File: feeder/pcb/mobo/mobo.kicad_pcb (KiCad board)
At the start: 2 copper layers, 149.5 x 70 mm, 26 parts, among them J1 SERIAL_BRIDGE, J2 Spring_Finger_Interface, J3 AVR-ISP-6, M1 Motor_DC, SW1 SW_Push, SW2 SW_Push, SW3 SW_Push, SW4 SW_SPDT, U1 ATmega328-AU, U2 VCNT2020, U3 DRV8838, Y1 Resonator_Small

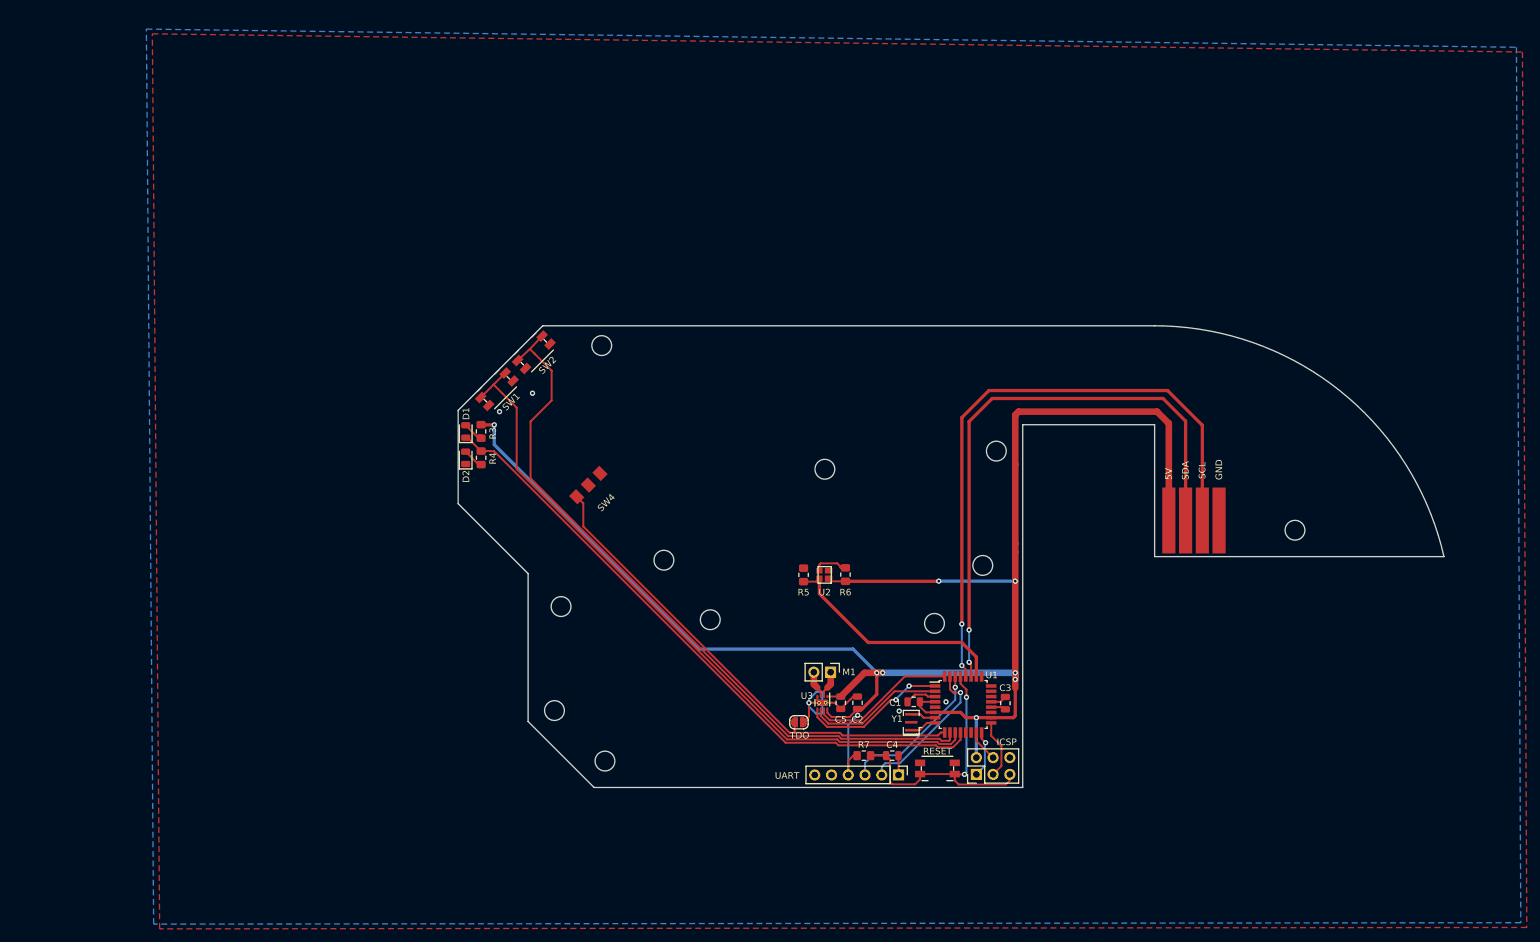
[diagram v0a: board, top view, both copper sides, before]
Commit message: first commit for stm32 feeder!
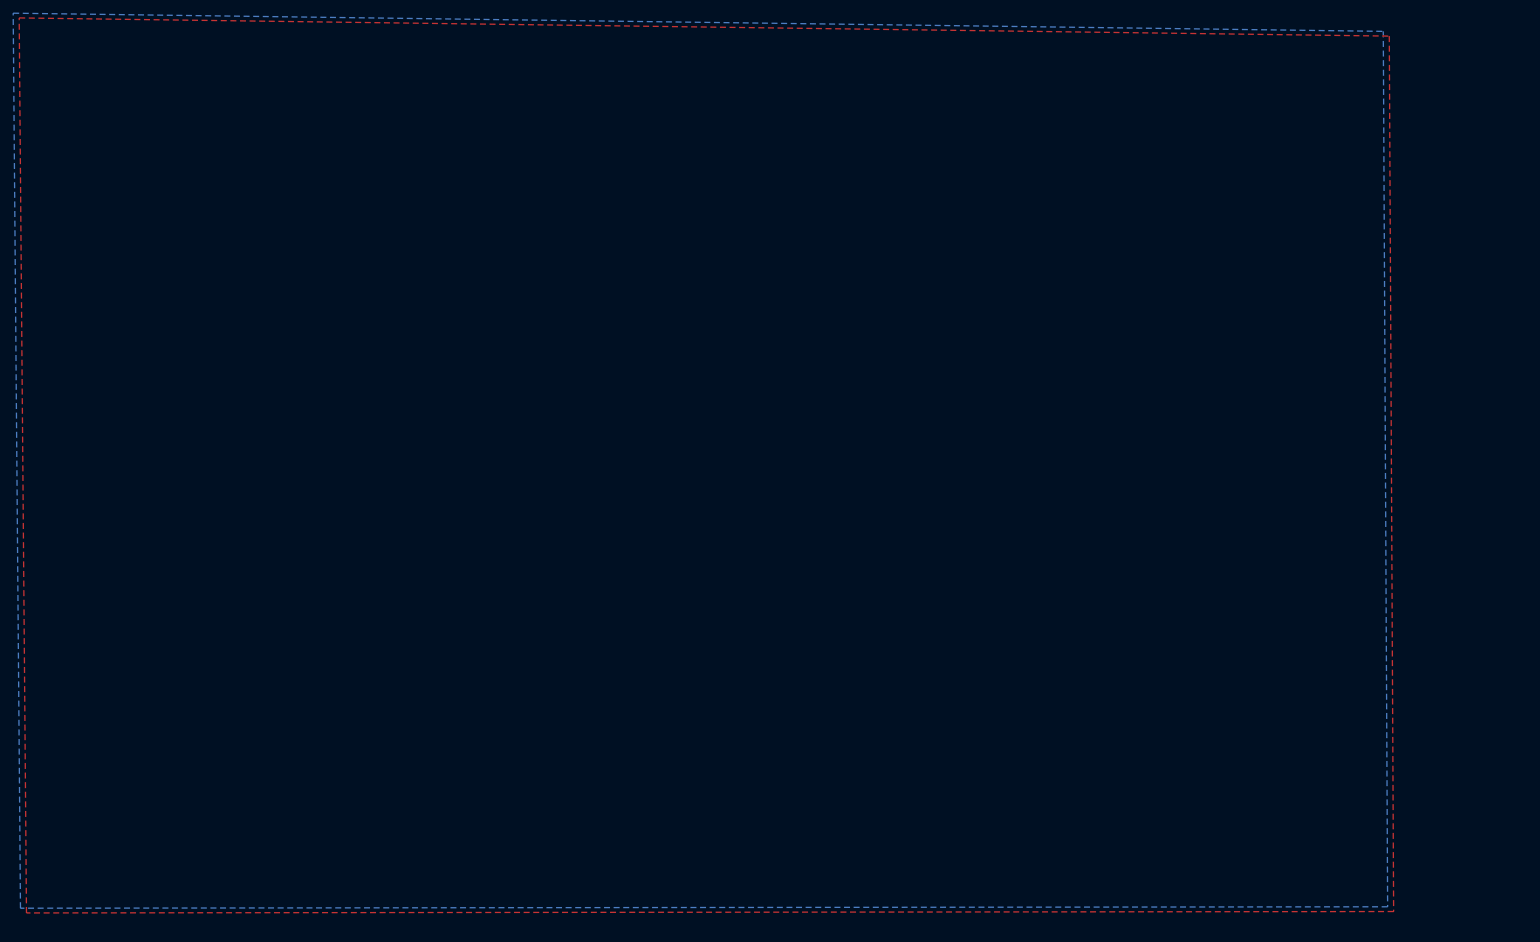
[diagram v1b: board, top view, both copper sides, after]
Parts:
- removed C1: 10uF, Capacitor_SMD:C_0805_2012Metric
- removed C2, C3, C4, C5: 0.1uF, Capacitor_SMD:C_0805_2012Metric
- removed D1: LED1, LED_SMD:LED_0805_2012Metric
- removed D2: LED2, LED_SMD:LED_0805_2012Metric
- removed G***: LOGO, stephen:stephenEmblem
- removed J1: SERIAL_BRIDGE, Connector_PinHeader_2.54mm:PinHeader_1x06_P2.54mm_Vertical
- removed J2: Spring_Finger_Interface, stephen:springFingerContactPads_4x
- removed J3: AVR-ISP-6, Connector_PinHeader_2.54mm:PinHeader_2x03_P2.54mm_Vertical
- removed JP1: TAPE_DETECT_OVERRIDE, Jumper:SolderJumper-2_P1.3mm_Open_RoundedPad1.0x1.5mm
- removed M1: Motor_DC, Connector_PinHeader_2.54mm:PinHeader_1x02_P2.54mm_Vertical
- removed R3, R4, R6: 470R, Resistor_SMD:R_0805_2012Metric_Pad1.15x1.40mm_HandSolder
- removed R5, R7: 10K, Resistor_SMD:R_0805_2012Metric_Pad1.15x1.40mm_HandSolder
- removed SW1, SW2, SW3: SW_Push, Button_Switch_SMD:Panasonic_EVQPUJ_EVQPUA
- removed SW4: SW_SPDT, stephen:MDS6500AL02SR
- removed U1: ATmega328-AU, Package_QFP:TQFP-32_7x7mm_P0.8mm
- removed U2: VCNT2020, stephen:VCNT2020
- removed U3: DRV8838, Package_SON:WSON-8-1EP_2x2mm_P0.5mm_EP0.9x1.6mm_ThermalVias
- removed Y1: Resonator_Small, Crystal:Resonator_SMD_muRata_CSTxExxV-3Pin_3.0x1.1mm
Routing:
- net +5V: track 273.6 -> 0.00 mm, vias 9 -> 0
- net SW2: track 108.8 -> 0.00 mm
- net SW1: track 104.7 -> 0.00 mm
- net LED1: track 96.8 -> 0.00 mm
- net SCL: track 93.9 -> 0.00 mm, vias 2 -> 0
- net SDA: track 89.1 -> 0.00 mm, vias 2 -> 0
- net LIMIT: track 74.7 -> 0.00 mm
- net RST: track 45.2 -> 0.00 mm, vias 2 -> 0
- net OPTO_SIG: track 35.6 -> 0.00 mm
- net GND: track 29.3 -> 0.00 mm, vias 5 -> 0
- net RX: track 23.0 -> 0.00 mm, vias 1 -> 0
- net TX: track 22.5 -> 0.00 mm, vias 1 -> 0
- net EN: track 22.3 -> 0.00 mm, vias 2 -> 0
- net nSLEEP: track 22.2 -> 0.00 mm
- net PH: track 20.9 -> 0.00 mm
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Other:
- board outline removed
- board text removed: "5V"
- board text removed: "FEEDER MOBO v0.2.0 2004XX Index PNP"
- board text removed: "GND"
- board text removed: "ICSP"
- board text removed: "RESET"
- board text removed: "SCL"
- board text removed: "SDA"
- board text removed: "TDO"
- board text removed: "UART"

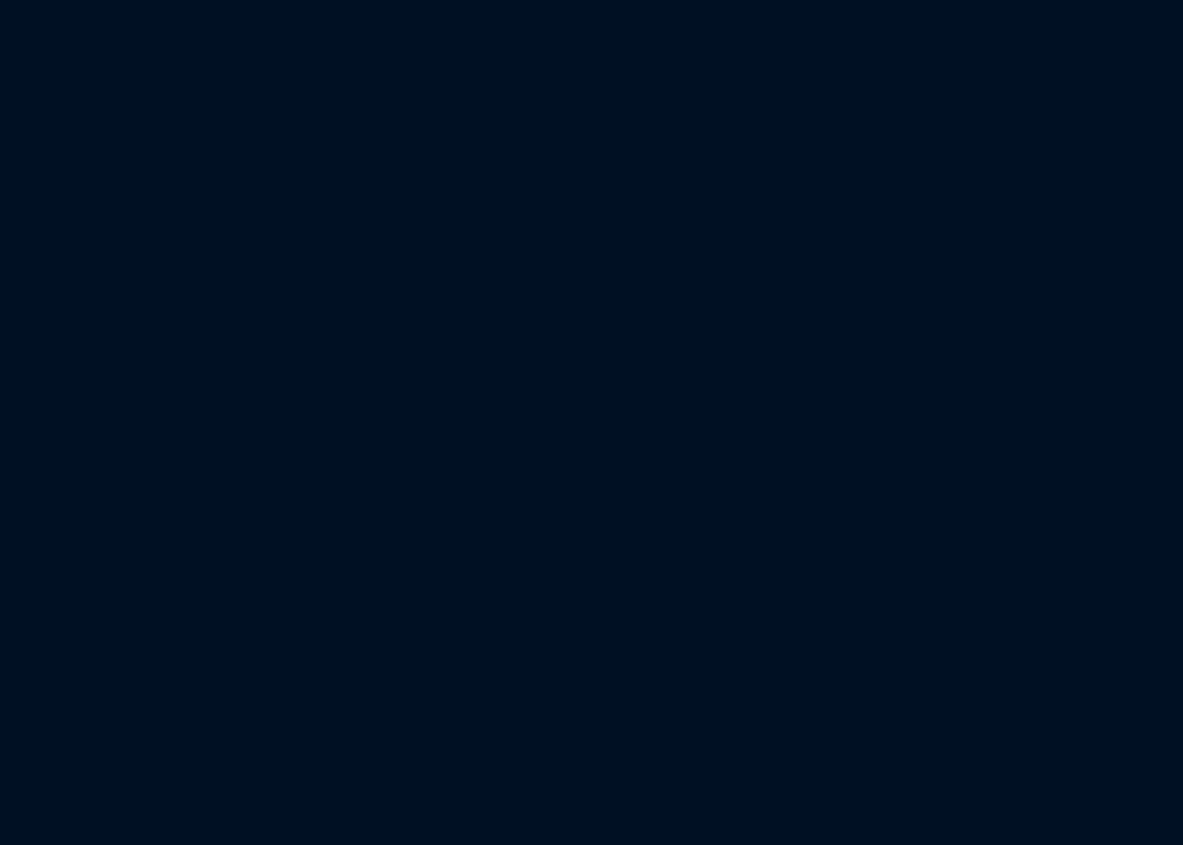
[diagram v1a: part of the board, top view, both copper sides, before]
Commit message: added footprint for limit switch
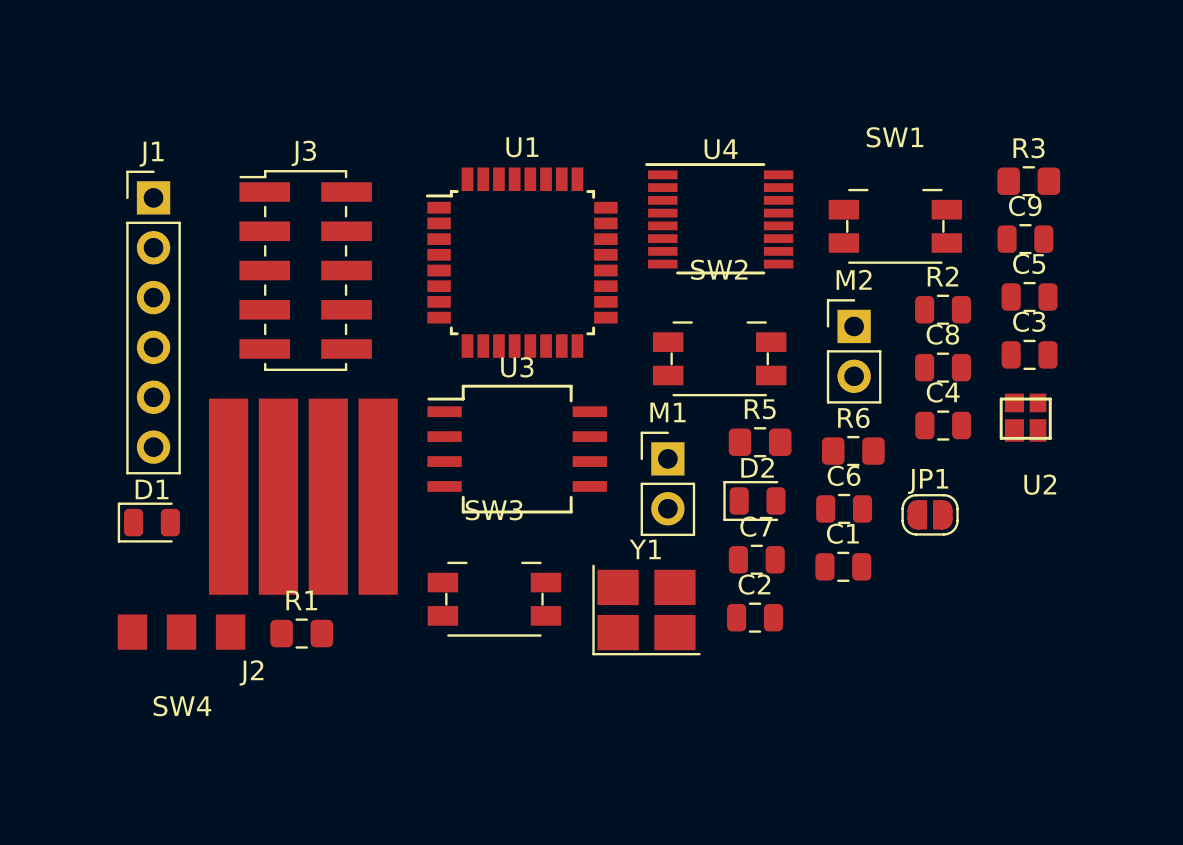
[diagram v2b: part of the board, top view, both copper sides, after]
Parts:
- added C1: 0.1uF, Capacitor_SMD:C_0805_2012Metric, F.Cu at (194.8, 158.6)
- added C2: 4.7uF, Capacitor_SMD:C_0805_2012Metric, F.Cu at (190.3, 161.2)
- added C3: 0.1uF, Capacitor_SMD:C_0805_2012Metric, F.Cu at (204.3, 147.8)
- added C4: 0.1uF, Capacitor_SMD:C_0805_2012Metric, F.Cu at (199.9, 151.4)
- added C5: 0.01uF, Capacitor_SMD:C_0805_2012Metric, F.Cu at (204.3, 144.9)
- added C6: 10pF, Capacitor_SMD:C_0805_2012Metric, F.Cu at (194.8, 155.7)
- added C7: 10pF, Capacitor_SMD:C_0805_2012Metric, F.Cu at (190.4, 158.3)
- added C8: 2.2uF, Capacitor_SMD:C_0805_2012Metric, F.Cu at (199.9, 148.5)
- added C9: 10uF, Capacitor_SMD:C_0805_2012Metric, F.Cu at (204.1, 141.9)
- added D1: LED1, LED_SMD:LED_0805_2012Metric, F.Cu at (159.5, 156.4)
- added D2: LED1, LED_SMD:LED_0805_2012Metric, F.Cu at (190.4, 155.3)
- added J1: SERIAL_BRIDGE, Connector_PinHeader_2.54mm:PinHeader_1x06_P2.54mm_Vertical, F.Cu at (159.6, 139.8)
- added J2: Spring_Finger_Interface, stephen:springFingerContactPads_4x, F.Cu at (167.3, 155.1)
- added J3: SWD_10, Connector_PinHeader_2.00mm:PinHeader_2x05_P2.00mm_Vertical_SMD, F.Cu at (167.4, 143.5)
- added JP1: TAPE_DETECT_OVERRIDE, Jumper:SolderJumper-2_P1.3mm_Open_RoundedPad1.0x1.5mm, F.Cu at (199.2, 156.0)
- added M1: DRIVE_MOTOR, Connector_PinHeader_2.54mm:PinHeader_1x02_P2.54mm_Vertical, F.Cu at (185.8, 153.1)
- added M2: PEEL_MOTOR, Connector_PinHeader_2.54mm:PinHeader_1x02_P2.54mm_Vertical, F.Cu at (195.3, 146.4)
- added R1: 470R, Resistor_SMD:R_0805_2012Metric_Pad1.15x1.40mm_HandSolder, F.Cu at (167.2, 162.0)
- added R2: R_Small, Resistor_SMD:R_0805_2012Metric, F.Cu at (199.9, 145.5)
- added R3: 470R, Resistor_SMD:R_0805_2012Metric_Pad1.15x1.40mm_HandSolder, F.Cu at (204.2, 139.0)
- added R5: 10K, Resistor_SMD:R_0805_2012Metric_Pad1.15x1.40mm_HandSolder, F.Cu at (190.5, 152.3)
- added R6: 470R, Resistor_SMD:R_0805_2012Metric_Pad1.15x1.40mm_HandSolder, F.Cu at (195.3, 152.7)
- added SW1: BUTTON_1, Button_Switch_SMD:Panasonic_EVQPUJ_EVQPUA, F.Cu at (197.4, 141.3)
- added SW2: BUTTON_2, Button_Switch_SMD:Panasonic_EVQPUJ_EVQPUA, F.Cu at (188.5, 148.0)
- added SW3: RESET_BUTTON, Button_Switch_SMD:Panasonic_EVQPUJ_EVQPUA, F.Cu at (177.0, 160.3)
- added SW4: TAPE_DETECT, stephen:MDS6500AL02SR, F.Cu at (158.6, 161.9)
- added U1: STM32F030K6Tx, Package_QFP:LQFP-32_7x7mm_P0.8mm, F.Cu at (178.4, 143.1)
- added U2: VCNT2020, stephen:VCNT2020, F.Cu at (202.8, 152.1)
- added U3: MAX3485, Package_SO:SO-8_5.3x6.2mm_P1.27mm, F.Cu at (178.2, 152.6)
- added U4: DRV8833PW, Package_SO:TSSOP-16_4.4x5mm_P0.65mm, F.Cu at (188.5, 140.9)
- added Y1: 8MHz, Crystal:Crystal_SMD_3225-4Pin_3.2x2.5mm_HandSoldering, F.Cu at (184.7, 160.8)

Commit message: started layout
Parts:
- removed J1: SERIAL_BRIDGE, Connector_PinHeader_2.54mm:PinHeader_1x06_P2.54mm_Vertical
- added C10: 10uF, Capacitor_SMD:C_0805_2012Metric, F.Cu at (147.6, 139.7)
- added C11: 10uF, Capacitor_SMD:C_0805_2012Metric, F.Cu at (147.4, 151.9)
- added C12: 0.01uF, Capacitor_SMD:C_0805_2012Metric, F.Cu at (143.7, 161.9)
- added C13: 1uF, Capacitor_SMD:C_0805_2012Metric, F.Cu at (143.7, 164.2)
- added JP2: FILM_TENSION, Jumper:SolderJumper-2_P1.3mm_Open_RoundedPad1.0x1.5mm, F.Cu at (167.8, 130.6)
- added R4: ?, Resistor_SMD:R_0805_2012Metric, F.Cu at (150.3, 108.1)
- added SW5: FILM_TENSION, index:K5-1624SA-01, F.Cu at (61.9, 80.2)
- added TP1: MCU_TX, TestPoint:TestPoint_Pad_D2.0mm, B.Cu at (170.6, 85.7)
- added TP2: MCU_RX, TestPoint:TestPoint_Pad_D2.0mm, B.Cu at (174.9, 80.0)
- added U5: AP1117-33, Package_TO_SOT_SMD:SOT-223-3_TabPin2, F.Cu at (147.2, 145.8)
- moved R3 176.0 mm to (36.6, 85.4), turned to 270 degrees
- moved SW1 175.6 mm to (34.2, 76.5), turned to 90 degrees
- moved D2 169.8 mm to (33.4, 90.7), turned to 90 degrees
- moved SW2 162.1 mm to (33.7, 99.7), turned to 90 degrees
- moved M2 159.8 mm to (44.8, 92.6), turned to 90 degrees
- moved R1 148.8 mm to (36.4, 91.0), turned to 270 degrees
- moved D1 144.6 mm to (33.6, 85.4), turned to 90 degrees
- moved U2 118.7 mm to (86.5, 128.3)
- moved SW4 114.4 mm to (51.1, 122.6), turned to 45 degrees
- moved R5 109.9 mm to (83.5, 127.3)
- moved R6 106.5 mm to (91.8, 127.4), turned to 180 degrees
- moved M1 100.7 mm to (86.0, 166.1), turned to 90 degrees
- moved C4 94.6 mm to (106.6, 167.1), turned to 270 degrees
- moved SW3 65.6 mm to (111.8, 167.2), turned to 180 degrees
- moved R2 64.2 mm to (137.9, 162.5), turned to 180 degrees
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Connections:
- U1 pad 26: Net-(U1-Pad26) -> LED1
- U1 pad 7: LED1 -> SLOT_DETECT
- U3 pad 1: Net-(U3-Pad1) -> MCU_RX
- U3 pad 2: Net-(U3-Pad2) -> RTS
- U3 pad 3: Net-(U3-Pad3) -> RTS
- U3 pad 4: Net-(U3-Pad4) -> MCU_TX
- U3 pad 8: Net-(U3-Pad8) -> +3V3
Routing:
- net SWDIO: track 0.00 -> 8.02 mm
- net SWCLK: track 0.00 -> 6.35 mm

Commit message: starting layout for feeder
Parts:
- removed J2: Spring_Finger_Interface, stephen:springFingerContactPads_4x
- added J1: SPRING_FINGER_INTERFACE, index:5-pad-spring-finger-interface, F.Cu at (151.0, 127.5)
- added TP3: MCU_RX, TestPoint:TestPoint_Pad_D2.0mm, F.Cu at (187.9, 146.6)
- added TP4: MCU_RX, TestPoint:TestPoint_Pad_D2.0mm, F.Cu at (192.8, 142.1)
- added TP5: MCU_RX, TestPoint:TestPoint_Pad_D2.0mm, F.Cu at (197.2, 139.2)
- R4: value ? -> 120R
- SW4: footprint stephen:MDS6500AL02SR -> index:K5-1624SA-01
- TP1, TP2: moved to F.Cu
- Y1: value 8MHz -> Crystal_GND24_Small
- moved JP1 223.9 mm to (-49.7, 158.1)
- moved JP2 219.7 mm to (-49.7, 161.7)
- moved C8 100.7 mm to (73.2, 160.8), turned to 270 degrees
- moved U4 96.4 mm to (75.2, 156.0), turned to 180 degrees
- moved C5 96.3 mm to (75.2, 160.8), turned to 90 degrees
- moved C9 94.7 mm to (77.2, 160.8), turned to 270 degrees
- moved C6 88.7 mm to (57.5, 140.0), turned to 90 degrees
- moved C12 88.6 mm to (55.8, 151.0), turned to 270 degrees
- moved C7 87.7 mm to (55.0, 140.0), turned to 90 degrees
- moved C13 86.9 mm to (57.8, 151.0), turned to 270 degrees
- moved Y1 85.6 mm to (56.2, 144.4)
- moved R2 82.4 mm to (56.8, 147.8)
- moved C3 80.8 mm to (61.0, 139.5), turned to 90 degrees
- moved U1 76.0 mm to (64.6, 147.0), turned to 0 degrees
- moved TP2 71.1 mm to (183.3, 150.6)
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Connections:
- Y1 pad 2: Net-(C7-Pad1) -> GND
- Y1 pad 3: (no net) -> Net-(C7-Pad1)
- Y1 pad 4: (no net) -> GND
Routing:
- net SWDIO: track 8.02 -> 0.00 mm
- net SWCLK: track 6.35 -> 0.00 mm
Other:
- board outline added: 160.6 x 110 mm

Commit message: layout and routing done, silkscreen placed. passing drc.
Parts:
- TP1, TP2, TP3, TP4, TP5: moved to B.Cu
- moved TP5 118.8 mm to (78.9, 149.8)
- moved JP2 110.7 mm to (57.2, 133.2)
- moved TP3 107.0 mm to (81.5, 157.9)
- moved JP1 105.5 mm to (52.8, 133.2)
- moved TP4 104.3 mm to (89.7, 157.9)
- moved TP2 102.4 mm to (81.4, 141.1)
- moved TP1 101.8 mm to (77.9, 143.7)
- moved C10 42.5 mm to (81.5, 154.0), turned to 180 degrees
- moved C11 42.3 mm to (81.5, 164.0)
- moved U5 34.2 mm to (81.5, 159.0)
- moved C4 34.1 mm to (76.5, 170.2), turned to 270 degrees
- moved SW3 31.1 mm to (81.8, 171.0)
- moved R1 18.4 mm to (43.2, 92.5), turned to 270 degrees
- moved D1 16.4 mm to (40.5, 87.8)
- moved R3 14.2 mm to (43.2, 87.8), turned to 270 degrees
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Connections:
- SW4 pad 1: Net-(SW4-Pad1) -> GND
- SW4 pad 2: TAPE_DETECT -> Net-(SW4-Pad2)
- SW4 pad 3: GND -> TAPE_DETECT
- SW5 pad 1: Net-(SW5-Pad1) -> GND
- SW5 pad 2: FILM_TENSION -> Net-(SW5-Pad2)
- SW5 pad 3: GND -> FILM_TENSION
- U1 pad 18: LED2 -> Net-(U1-Pad18)
- U1 pad 7: SLOT_DETECT -> Net-(U1-Pad7)
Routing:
- net +3V3: track 0.00 -> 268.7 mm, vias 0 -> 6
- net SLOT_DETECT: track 0.00 -> 161.8 mm, vias 0 -> 2
- net +5V: track 0.00 -> 159.1 mm, vias 0 -> 3
- net MCU_RX: track 0.00 -> 119.3 mm, vias 0 -> 1
- net MCU_TX: track 0.00 -> 119.2 mm, vias 0 -> 1
- net RTS: track 0.00 -> 117.3 mm
- net FILM_TENSION: track 0.00 -> 97.1 mm, vias 0 -> 5
- net SW1: track 0.00 -> 91.0 mm, vias 0 -> 2
- net TAPE_DETECT: track 0.00 -> 84.0 mm, vias 0 -> 3
- net SW2: track 0.00 -> 74.6 mm, vias 0 -> 2
- net Net-(M2-Pad1): track 0.00 -> 71.3 mm, vias 0 -> 4
- net Net-(M2-Pad2): track 0.00 -> 71.0 mm, vias 0 -> 4
- net LED2: track 0.00 -> 69.5 mm, vias 0 -> 2
- net LED1: track 0.00 -> 66.4 mm, vias 0 -> 2
- net RESET: track 0.00 -> 55.5 mm, vias 0 -> 3
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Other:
- outline, holes or cut-outs redrawn

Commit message: added logo, version text, last bits of cleaning up. this commit is what got ordered
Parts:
- added G***: LOGO, index:logo, F.Cu at (114.2, 169.1)
- added REF**: KiCad-Logo2_5mm_Copper, Symbol:KiCad-Logo2_5mm_Copper, F.Cu at (119.8, 161.8)
- moved J1 0.19 mm to (151.1, 127.4)
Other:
- board text added: "FEEDER-REV03 S.HAWES 2009XX INDEX MACHINES"
- board text added: "FT"
- board text added: "RESET"
- board text added: "TD"
